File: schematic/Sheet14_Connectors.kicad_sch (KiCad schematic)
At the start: 5 parts, among them J1 JTAG, J2 SPW_TX, J3 SPW_RX, J4 POWER, J5 UART

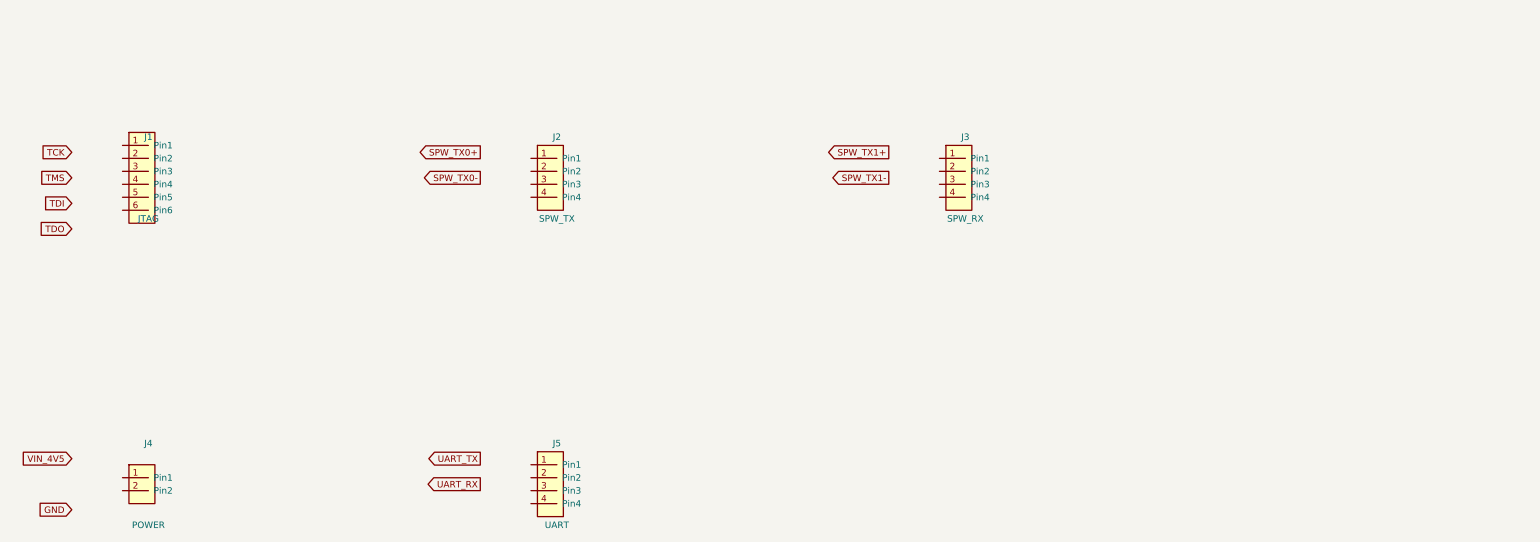
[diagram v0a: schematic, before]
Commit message: feat: real IC schematics with proper pin connections
- ADC12DJ5200-SP: 20 left pins (power, SPI, analog) + 21 right pins (JESD204C)
- XQRVC1902-SP: 19 left pins (power) + 30 right pins (JTAG, SPW, JESD, config)
- TPS7H5002-SP: 9 left + 7 right pins (buck converter 1.0V core)
- ISL70003ASEH: 7 left + 5 right (buck 1.8V/3.3V)
- LMX2615-SP: 8+8 pins (PLL synthesizer)
- LMK04832-SP: 12+12 pins (clock distributor)
- TPS7H1111-SP / TPS7H1121-SP: 3+3 pins (LDOs)
- TPS7H3014-SP: 4+4 pins (sequencer)
- INA214-SP: 3+2 pins (current sense)
- CVHD-950: 3+2 pins (VCXO)

Sheets:
- 02: SMA→50Ω match→anti-alias→ADC analog input
- 03: ADC decoupling, JESD outputs, SPI control
- 04: FPGA 14x decoupling caps, JTAG, SPW, JESD
- 05: Crystek→LMX2615→LMK04832→ADC+FPGA clock tree
- 06-09: Power input, TPS7H5002 buck 1.0V, ISL70003A buck 1.8V/3.3V
- 10-12: LDO 1.0V analog, 1.8V digital, 2.5V clock
- 13: 2x TPS7H3014 power sequencer
- 14: JTAG/SPW/UART connectors
- 15-17: Test points, decoupling, power tree diagram

All 17 sheets export via kicad-cli, merged PDF: 1.1MB
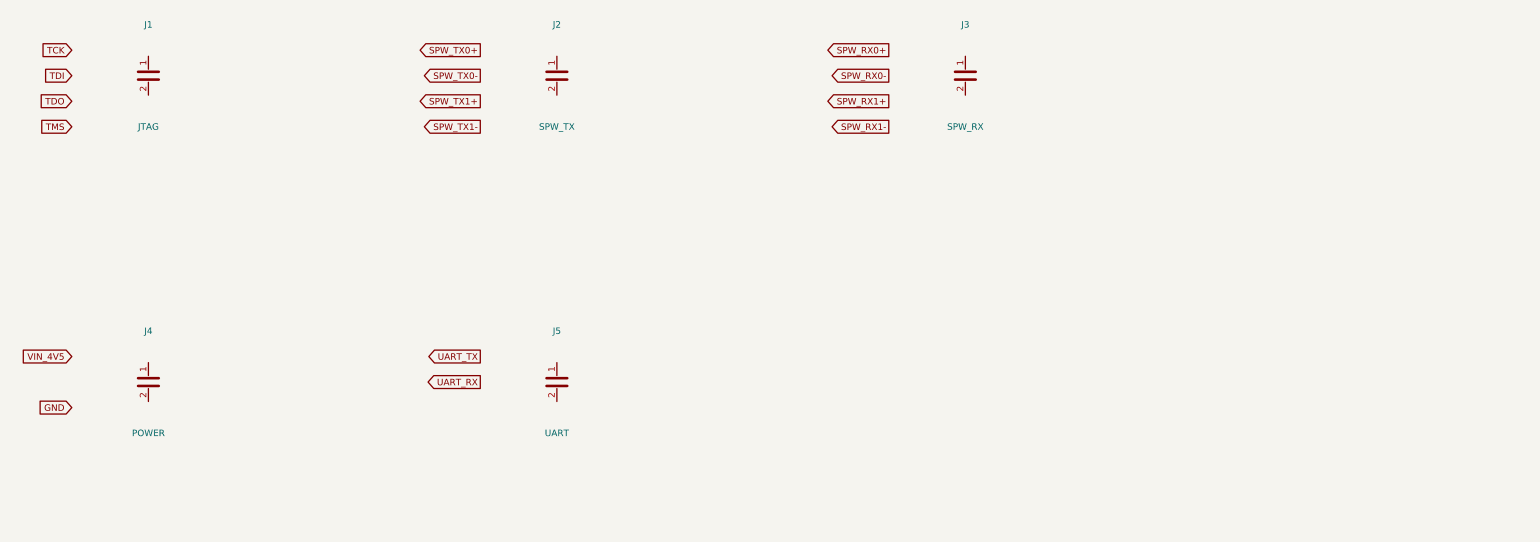
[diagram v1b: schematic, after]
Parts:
- removed J1: JTAG, Connector_PinHeader_2.54mm:PinHeader_1x06_P2.54mm_Vertical, symbol Connector_Generic:Conn_01x06
- removed J2: SPW_TX, Connector_PinHeader_2.54mm:PinHeader_1x04_P2.54mm_Vertical, symbol Connector_Generic:Conn_01x04
- removed J3: SPW_RX, Connector_PinHeader_2.54mm:PinHeader_1x04_P2.54mm_Vertical, symbol Connector_Generic:Conn_01x04
- removed J4: POWER, TerminalBlock:TerminalBlock_bornier-2_P5.08mm, symbol Connector_Generic:Conn_01x02
- removed J5: UART, Connector_PinHeader_2.54mm:PinHeader_1x04_P2.54mm_Vertical, symbol Connector_Generic:Conn_01x04
- added J1: JTAG, Conn_01x06, symbol Device:C
- added J2: SPW_TX, Conn_01x04, symbol Device:C
- added J3: SPW_RX, Conn_01x04, symbol Device:C
- added J4: POWER, Conn_01x02, symbol Device:C
- added J5: UART, Conn_01x04, symbol Device:C
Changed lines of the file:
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@@
     (rev "1.0")
   )
-  (symbol (lib_id "Connector_Generic:Conn_01x06") (at 60 80 0) (unit 1)
+  (symbol (lib_id "Device:C") (at 60 60 0) (unit 1)
     (in_bom yes) (on_board yes)
-    (property "Reference" "J1" (at 60 72 0) (effects (font (size 1.27 1.27))))
-    (property "Value" "JTAG" (at 60 88 0) (effects (font (size 1.27 1.27))))
-    (property "Footprint" "Connector_PinHeader_2.54mm:PinHeader_1x06_P2.54mm_Vertical" (at 60 80 0) (effects (font (size 1.27 1.27)) hide))
-    (pin "1")
-    (pin "2")
-    (pin "3")
-    (pin "4")
-    (pin "5")
-    (pin "6")
-  )
-  (symbol (lib_id "Connector_Generic:Conn_01x04") (at 140 80 0) (unit 1)
-    (in_bom yes) (on_board yes)
-    (property "Reference" "J2" (at 140 72 0) (effects (font (size 1.27 1.27))))
-    (property "Value" "SPW_TX" (at 140 88 0) (effects (font (size 1.27 1.27))))
-    (property "Footprint" "Connector_PinHeader_2.54mm:PinHeader_1x04_P2.54mm_Vertical" (at 140 80 0) (effects (font (size 1.27 1.27)) hide))
-    (pin "1")
-    (pin "2")
-    (pin "3")
-    (pin "4")
-  )
-  (symbol (lib_id "Connector_Generic:Conn_01x04") (at 220 80 0) (unit 1)
-    (in_bom yes) (on_board yes)
-    (property "Reference" "J3" (at 220 72 0) (effects (font (size 1.27 1.27))))
-    (property "Value" "SPW_RX" (at 220 88 0) (effects (font (size 1.27 1.27))))
-    (property "Footprint" "Connector_PinHeader_2.54mm:PinHeader_1x04_P2.54mm_Vertical" (at 220 80 0) (effects (font (size 1.27 1.27)) hide))
-    (pin "1")
-    (pin "2")
-    (pin "3")
-    (pin "4")
-  )
-  (symbol (lib_id "Connector_Generic:Conn_01x02") (at 60 140 0) (unit 1)
-    (in_bom yes) (on_board yes)
-    (property "Reference" "J4" (at 60 132 0) (effects (font (size 1.27 1.27))))
-    (property "Value" "POWER" (at 60 148 0) (effects (font (size 1.27 1.27))))
-    (property "Footprint" "TerminalBlock:TerminalBlock_bornier-2_P5.08mm" (at 60 140 0) (effects (font (size 1.27 1.27)) hide))
+    (property "Reference" "J1" (at 60 50 0) (effects (font (size 1.27 1.27))))
+    (property "Value" "JTAG" (at 60 70 0) (effects (font (size 1.27 1.27))))
+    (property "Footprint" "Conn_01x06" (at 60 60 0) (effects (font (size 1.27 1.27)) hide))
     (pin "1")
     (pin "2")
   )
-  (symbol (lib_id "Connector_Generic:Conn_01x04") (at 140 140 0) (unit 1)
+  (symbol (lib_id "Device:C") (at 140 60 0) (unit 1)
     (in_bom yes) (on_board yes)
-    (property "Reference" "J5" (at 140 132 0) (effects (font (size 1.27 1.27))))
-    (property "Value" "UART" (at 140 148 0) (effects (font (size 1.27 1.27))))
-    (property "Footprint" "Connector_PinHeader_2.54mm:PinHeader_1x04_P2.54mm_Vertical" (at 140 140 0) (effects (font (size 1.27 1.27)) hide))
+    (property "Reference" "J2" (at 140 50 0) (effects (font (size 1.27 1.27))))
+    (property "Value" "SPW_TX" (at 140 70 0) (effects (font (size 1.27 1.27))))
+    (property "Footprint" "Conn_01x04" (at 140 60 0) (effects (font (size 1.27 1.27)) hide))
     (pin "1")
     (pin "2")
-    (pin "3")
-    (pin "4")
   )
-  (global_label "TCK" (shape input) (at 45 75 180) (effects (font (size 1.27 1.27)) (justify right)))
-  (global_label "TMS" (shape input) (at 45 80 180) (effects (font (size 1.27 1.27)) (justify right)))
-  (global_label "TDI" (shape input) (at 45 85 180) (effects (font (size 1.27 1.27)) (justify right)))
-  (global_label "TDO" (shape input) (at 45 90 180) (effects (font (size 1.27 1.27)) (justify right)))
-  (global_label "SPW_TX0+" (shape output) (at 125 75 180) (effects (font (size 1.27 1.27)) (justify right)))
-  (global_label "SPW_TX0-" (shape output) (at 125 80 180) (effects (font (size 1.27 1.27)) (justify right)))
-  (global_label "SPW_TX1+" (shape output) (at 205 75 180) (effects (font (size 1.27 1.27)) (justify right)))
-  (global_label "SPW_TX1-" (shape output) (at 205 80 180) (effects (font (size 1.27 1.27)) (justify right)))
-  (global_label "VIN_4V5" (shape input) (at 45 135 180) (effects (font (size 1.27 1.27)) (justify right)))
-  (global_label "GND" (shape input) (at 45 145 180) (effects (font (size 1.27 1.27)) (justify right)))
-  (global_label "UART_TX" (shape output) (at 125 135 180) (effects (font (size 1.27 1.27)) (justify right)))
-  (global_label "UART_RX" (shape output) (at 125 140 180) (effects (font (size 1.27 1.27)) (justify right)))
+  (symbol (lib_id "Device:C") (at 220 60 0) (unit 1)
+    (in_bom yes) (on_board yes)
+    (property "Reference" "J3" (at 220 50 0) (effects (font (size 1.27 1.27))))
+    (property "Value" "SPW_RX" (at 220 70 0) (effects (font (size 1.27 1.27))))
+    (property "Footprint" "Conn_01x04" (at 220 60 0) (effects (font (size 1.27 1.27)) hide))
+    (pin "1")
+    (pin "2")
+  )
+  (symbol (lib_id "Device:C") (at 60 120 0) (unit 1)
+    (in_bom yes) (on_board yes)
+    (property "Reference" "J4" (at 60 110 0) (effects (font (size 1.27 1.27))))
+    (property "Value" "POWER" (at 60 130 0) (effects (font (size 1.27 1.27))))
+    (property "Footprint" "Conn_01x02" (at 60 120 0) (effects (font (size 1.27 1.27)) hide))
+    (pin "1")
+    (pin "2")
+  )
+  (symbol (lib_id "Device:C") (at 140 120 0) (unit 1)
+    (in_bom yes) (on_board yes)
+    (property "Reference" "J5" (at 140 110 0) (effects (font (size 1.27 1.27))))
+    (property "Value" "UART" (at 140 130 0) (effects (font (size 1.27 1.27))))
+    (property "Footprint" "Conn_01x04" (at 140 120 0) (effects (font (size 1.27 1.27)) hide))
+    (pin "1")
+    (pin "2")
+  )
+  (global_label "TCK" (shape input) (at 45 55 180) (effects (font (size 1.27 1.27)) (justify right)))
+  (global_label "TDI" (shape input) (at 45 60 180) (effects (font (size 1.27 1.27)) (justify right)))
+  (global_label "TDO" (shape input) (at 45 65 180) (effects (font (size 1.27 1.27)) (justify right)))
+  (global_label "TMS" (shape input) (at 45 70 180) (effects (font (size 1.27 1.27)) (justify right)))
+  (global_label "SPW_TX0+" (shape output) (at 125 55 180) (effects (font (size 1.27 1.27)) (justify right)))
+  (global_label "SPW_TX0-" (shape output) (at 125 60 180) (effects (font (size 1.27 1.27)) (justify right)))
+  (global_label "SPW_TX1+" (shape output) (at 125 65 180) (effects (font (size 1.27 1.27)) (justify right)))
+  (global_label "SPW_TX1-" (shape output) (at 125 70 180) (effects (font (size 1.27 1.27)) (justify right)))
+  (global_label "SPW_RX0+" (shape output) (at 205 55 180) (effects (font (size 1.27 1.27)) (justify right)))
+  (global_label "SPW_RX0-" (shape output) (at 205 60 180) (effects (font (size 1.27 1.27)) (justify right)))
+  (global_label "SPW_RX1+" (shape output) (at 205 65 180) (effects (font (size 1.27 1.27)) (justify right)))
+  (global_label "SPW_RX1-" (shape output) (at 205 70 180) (effects (font (size 1.27 1.27)) (justify right)))
+  (global_label "VIN_4V5" (shape input) (at 45 115 180) (effects (font (size 1.27 1.27)) (justify right)))
+  (global_label "GND" (shape input) (at 45 125 180) (effects (font (size 1.27 1.27)) (justify right)))
+  (global_label "UART_TX" (shape output) (at 125 115 180) (effects (font (size 1.27 1.27)) (justify right)))
+  (global_label "UART_RX" (shape output) (at 125 120 180) (effects (font (size 1.27 1.27)) (justify right)))
   (sheet_instances (path "/" (page "1")))
 )
